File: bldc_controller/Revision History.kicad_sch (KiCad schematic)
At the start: 0 parts

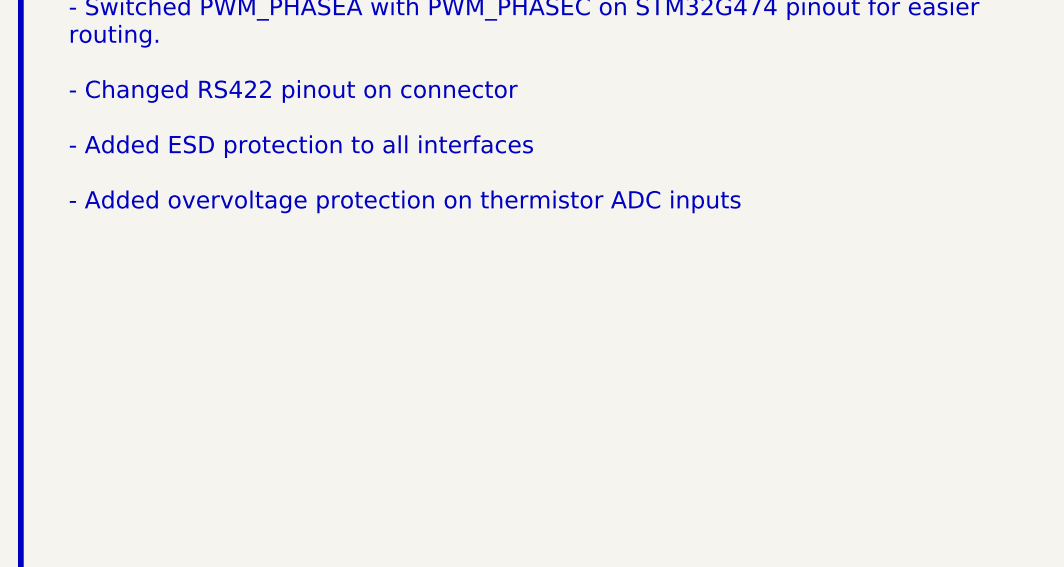
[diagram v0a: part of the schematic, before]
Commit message: schematic is complete. Replaced 5V buck and added pi filters.
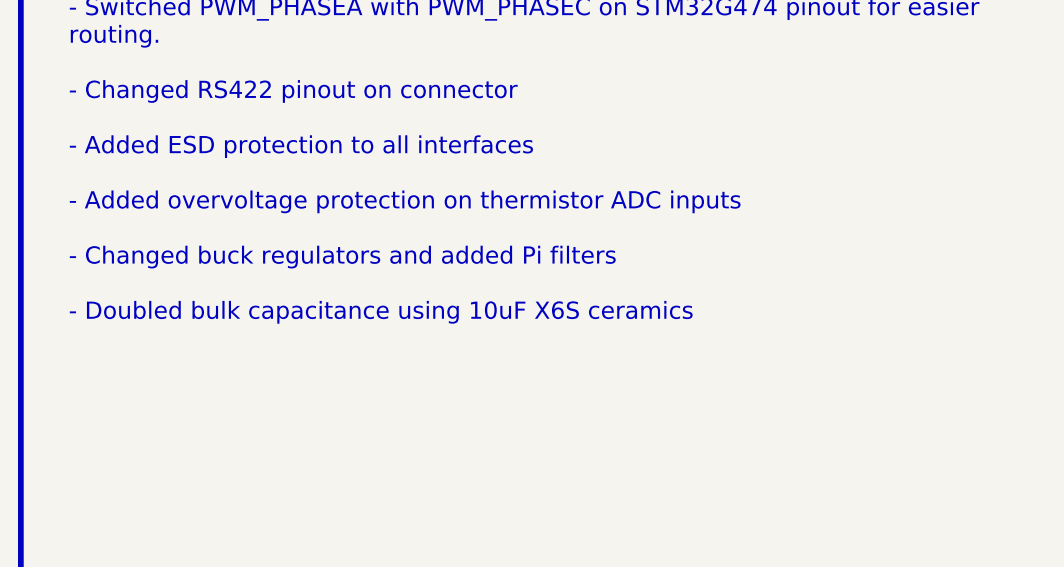
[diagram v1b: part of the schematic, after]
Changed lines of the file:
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@@
     (effects (font (face "Times New Roman") (size 6 6) (thickness 1.2) bold (color 162 22 34 1)))
   )
-  (text_box "Rev 1.0\n\n- Changed CPH-CPL capacitor to 47nF (gate driver)\n\n- Changed FD-CAN transceiver IC\n\n- Added TVS protection and termination switch to FD-CAN\n\n- Added low-side switched 12V 600mA source for external fan\n\n- Added LDO for analog supply\n\n- Changed input power TVS diode to bidirectional and added one diode per connector\n\n- Moved SOx low-pass filter to MCU section. \nShould be placed near MCU to avoid noise coupling into ADC lines.\n\n- Added second onboard I2C magnetic encoder for disambiguation.\n\n- Switched PWM_PHASEA with PWM_PHASEC on STM32G474 pinout for easier routing.\n\n- Changed RS422 pinout on connector\n\n- Added ESD protection to all interfaces\n\n- Added overvoltage protection on thermistor ADC inputs"
+  (text_box "Rev 1.0\n\n- Changed CPH-CPL capacitor to 47nF (gate driver)\n\n- Changed FD-CAN transceiver IC\n\n- Added TVS protection and termination switch to FD-CAN\n\n- Added low-side switched 12V 600mA source for external fan\n\n- Added LDO for analog supply\n\n- Changed input power TVS diode to bidirectional and added one diode per connector\n\n- Moved SOx low-pass filter to MCU section. \nShould be placed near MCU to avoid noise coupling into ADC lines.\n\n- Added second onboard I2C magnetic encoder for disambiguation.\n\n- Switched PWM_PHASEA with PWM_PHASEC on STM32G474 pinout for easier routing.\n\n- Changed RS422 pinout on connector\n\n- Added ESD protection to all interfaces\n\n- Added overvoltage protection on thermistor ADC inputs\n\n- Changed buck regulators and added Pi filters\n\n- Doubled bulk capacitance using 10uF X6S ceramics"
     (at 22.86 31.75 0) (size 124.46 129.54)
     (stroke (width -0.0001) (type default))
